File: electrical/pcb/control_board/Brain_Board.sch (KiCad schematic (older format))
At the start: 46 parts, among them J22 S9175-ND_rpi_breakout, J23 S9175-ND_rpi_breakout, J24 6posheader, J25 SSW-104-01-F-T, J26 WM6548-ND, J27 PPTC021LFBN-RC, J28 PPTC021LFBN-RC, J29 PPTC021LFBN-RC, J30 PEC08SAAN, M1 Mounting_Holes, Q1 2N3906, Q2 2N3906, Q3 2N3906, SW1 CT206124-ND, T13 test_point, T14 test_point, T15 test_point, U6 DC7G3HWA

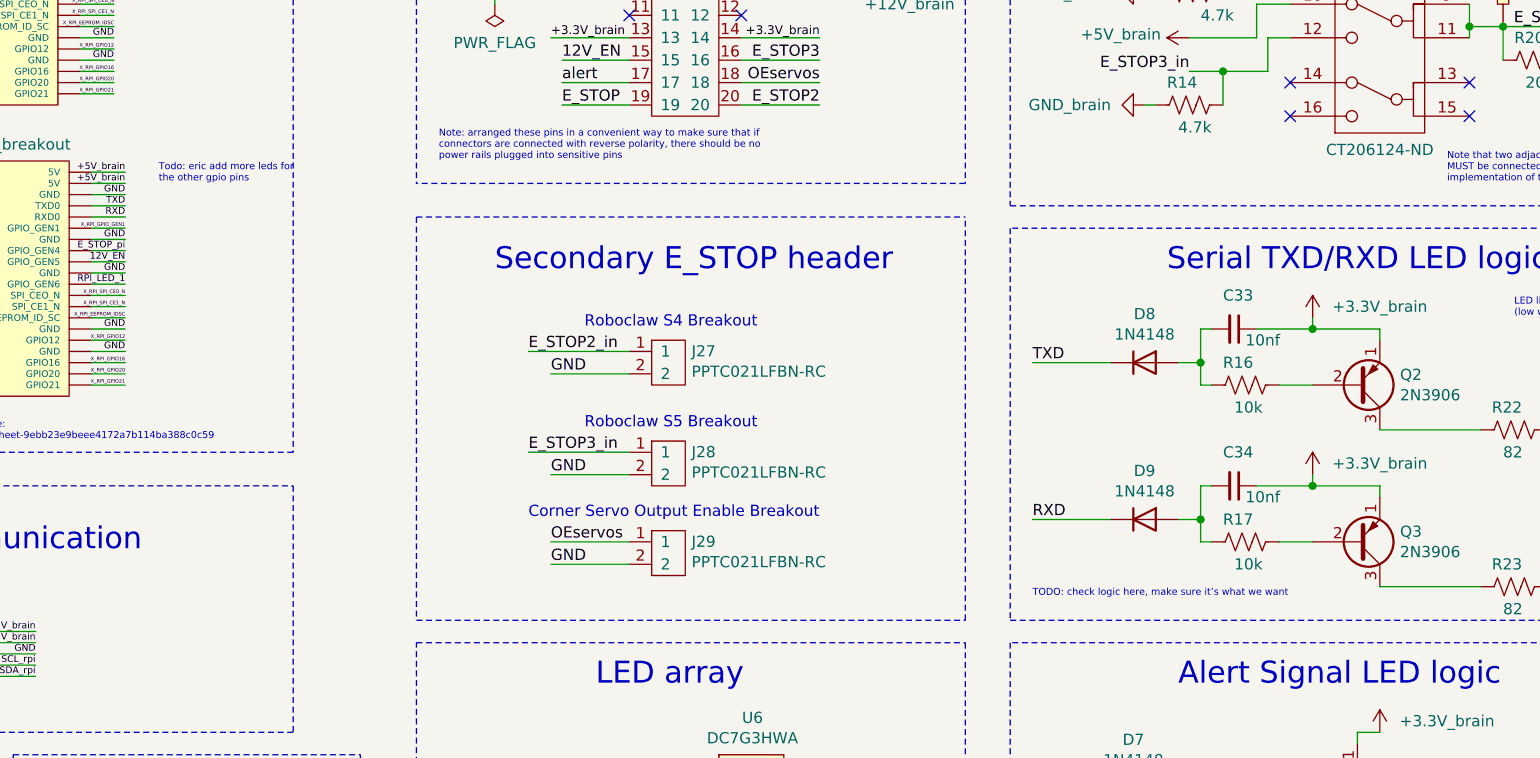
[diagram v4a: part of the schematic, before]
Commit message: deleting some todos
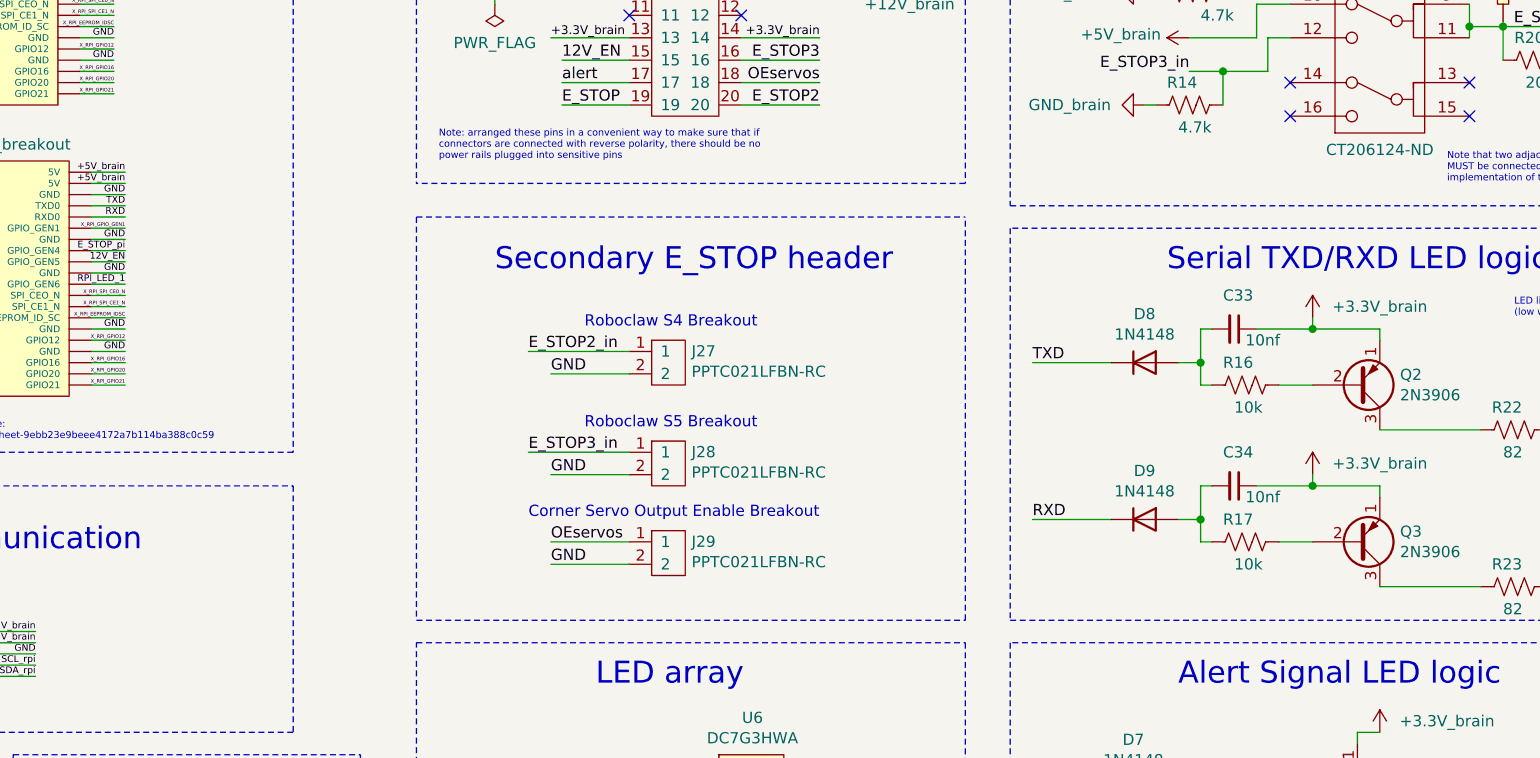
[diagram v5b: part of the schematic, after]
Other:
- note removed: "Todo: eric add more leds for \nthe other gpio pins"
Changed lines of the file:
@@
 Wire Wire Line
 	7900 2600 8200 2600
-Text Notes 3300 3250 0    31   ~ 0
-Todo: eric add more leds for \nthe other gpio pins
 Text Notes 9800 1500 0    31   ~ 0
 - Roboclaw ESTOPs active low \n(emergency stop when pulled low)\n- LEDs off when estop’ed (nominal on)
 Text Notes 7200 1450 0    31   ~ 0
 TODO: check logic here, make sure it’s what we want
-Text Notes 7200 5100 0    31   ~ 0
-TODO: check logic here, make sure it’s what we want
 $Comp

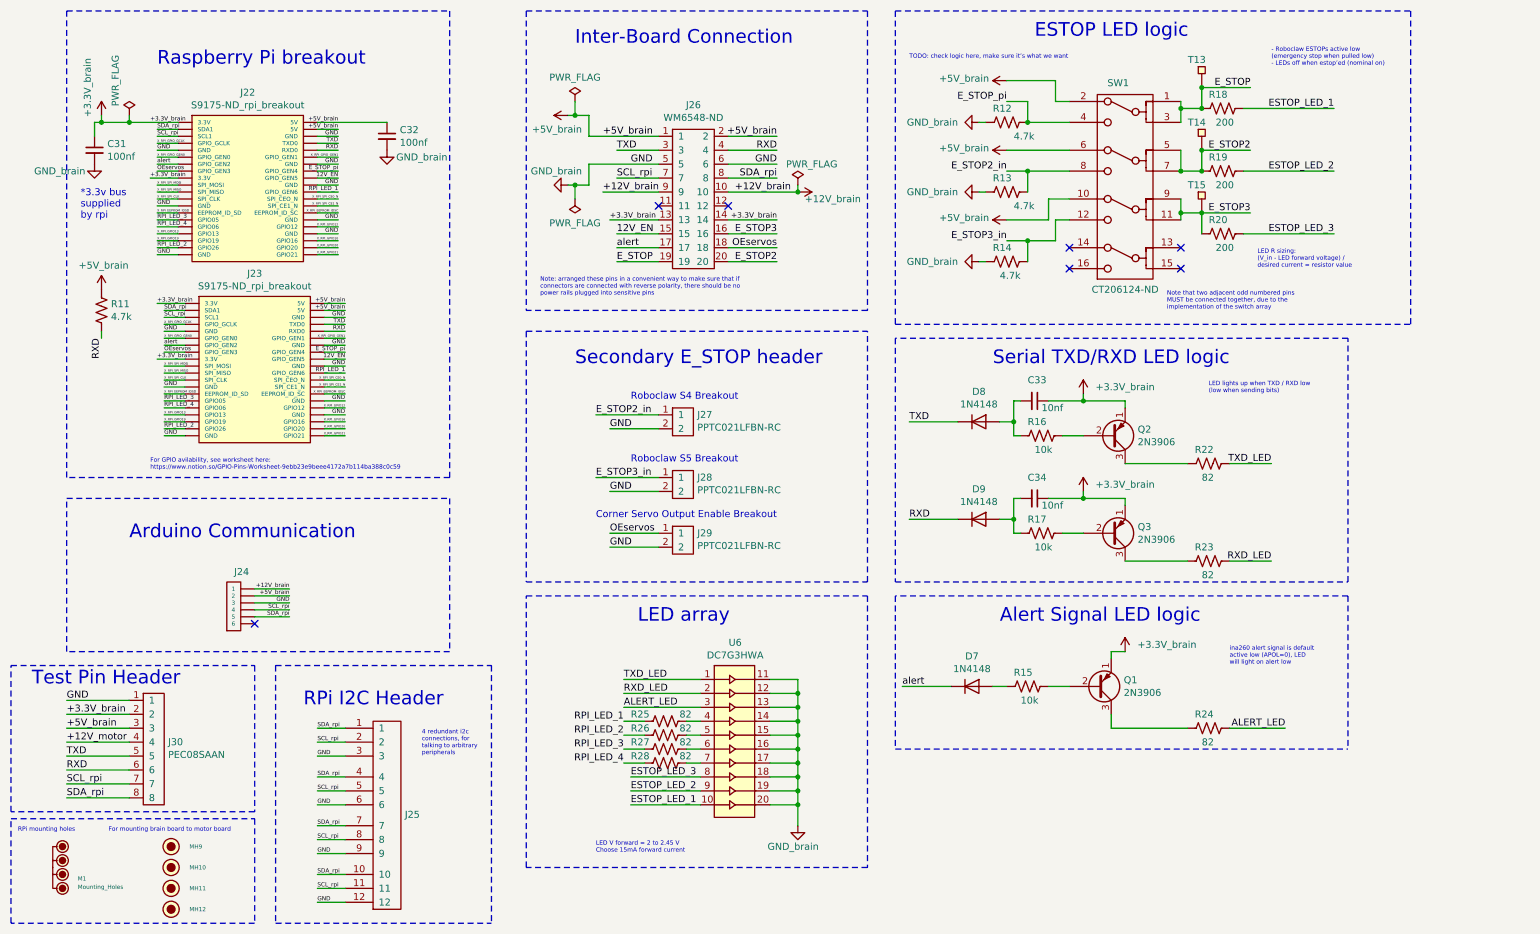
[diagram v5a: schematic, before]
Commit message: Moved alert LED to motor board, and moved estop pulldowns to have as an "option 2"
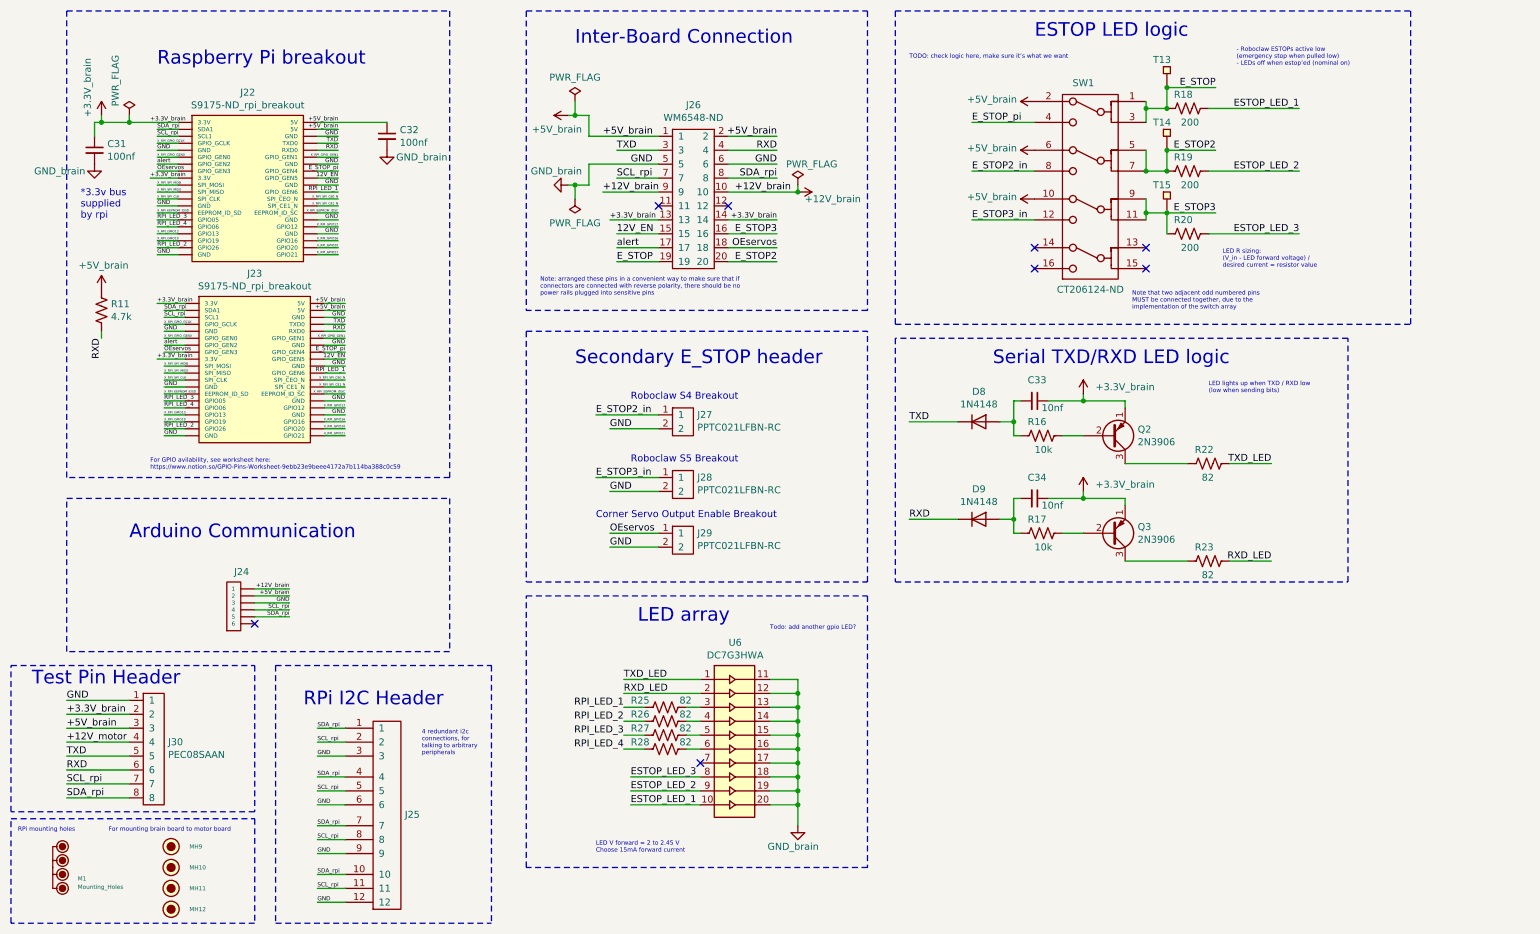
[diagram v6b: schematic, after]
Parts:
- removed D7: 1N4148, Diode_THT:D_DO-35_SOD27_P7.62mm_Horizontal, symbol Diode:1N4148
- removed Q1: 2N3906, Package_TO_SOT_THT:TO-92_Inline, symbol Transistor_BJT:2N3906
- removed R12, R13, R14: 4.7k, Resistor_THT:R_Axial_DIN0207_L6.3mm_D2.5mm_P7.62mm_Horizontal, symbol Device:R_US
- removed R15: 10k, Resistor_THT:R_Axial_DIN0207_L6.3mm_D2.5mm_P7.62mm_Horizontal, symbol Device:R_US
- removed R24: 82, Resistor_THT:R_Axial_DIN0207_L6.3mm_D2.5mm_P7.62mm_Horizontal, symbol Device:R_US
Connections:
- net ALERT_LED is gone; now on an unnamed net: U6.3
- net at R25.1: no longer U6.4
- net at R26.1: now also U6.4; no longer U6.5
- net at R27.1: now also U6.5; no longer U6.6
- net at R28.1: now also U6.6; no longer U6.7
- no-connect marks 7 -> 8
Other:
- note added: "Todo: add another gpio LED?"
- note removed: "Alert Signal LED logic"
- note removed: "ina260 alert signal is default \nactive low (APOL=0), LED \nwill light on alert low"
- moved on the sheet: R18, R19, R20, R25, R26, R27, R28, SW1, T13, T14, T15

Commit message: adding some notes from thursday convo
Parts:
- added Q?: 2N3906, Package_TO_SOT_THT:TO-92_Inline, symbol Transistor_BJT:2N3906
- added R?: 10k, Resistor_THT:R_Axial_DIN0207_L6.3mm_D2.5mm_P7.62mm_Horizontal, symbol Device:R_US
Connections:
- net +5V_brain: now also SW1.12 (out3_2), SW1.4 (out1_2), SW1.8 (out2_2); no longer SW1.10 (out3_1), SW1.2 (out1_1), SW1.6 (out2_1)
- net E_STOP: now also R?.2; no longer R18.2
- net E_STOP2_in: now also SW1.6 (out2_1); no longer SW1.8 (out2_2)
- net E_STOP3_in: now also SW1.10 (out3_1); no longer SW1.12 (out3_2)
- net E_STOP_pi: now also SW1.2 (out1_1); no longer SW1.4 (out1_2)
- new net: Q?.3 (C), R18.2
- new net: Q?.2 (B), R?.1
- new net 5v: Q?.1 (E)
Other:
- note added: "TODO: change left side to 3.3v?"
- note added: "TODO: use transistors for all 3 here"
- note added: "todo: use this setup for all LEDs driven by the PI. Basically pi is the ground/sink. LEDs will be default on when the pi turns on"
- note removed: "TODO: check logic here, make sure it’s what we want"
- moved on the sheet: R18
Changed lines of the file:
@@
 Wire Notes Line
 	4450 3400 6900 3400
-Text Label 7650 1900 0    50   ~ 0
+Text Label 7650 1750 0    50   ~ 0
 E_STOP_pi
 Wire Wire Line
@@
 Text Label 9400 2100 2    50   ~ 0
 E_STOP2
-Text Label 7650 2250 0    50   ~ 0
+Text Label 7650 2100 0    50   ~ 0
 E_STOP2_in
 Wire Wire Line
@@
 Text Label 9400 2550 2    50   ~ 0
 E_STOP3
-Text Label 7650 2600 0    50   ~ 0
+Text Label 7650 2450 0    50   ~ 0
 E_STOP3_in
 Wire Wire Line
@@
 L Device:R_US R?
 U 1 1 613A416D
-P 9200 1800
+P 10850 1850
 AR Path="/613A416D" Ref="R?"  Part="1"
 AR Path="/60A51BAC/613A416D" Ref="R?"  Part="1"
 AR Path="/60A5279E/613A416D" Ref="R18"  Part="1"
-F 0 "R18" V 9100 1700 50  0000 L CNN
-F 1 "200" V 9300 1750 50  0000 L CNN
-F 2 "Resistor_THT:R_Axial_DIN0207_L6.3mm_D2.5mm_P7.62mm_Horizontal" V 9240 1790 50  0001 C CNN
-F 3 "~" H 9200 1800 50  0001 C CNN
-	1    9200 1800
+F 0 "R18" V 10750 1750 50  0000 L CNN
+F 1 "200" V 10950 1800 50  0000 L CNN
+F 2 "Resistor_THT:R_Axial_DIN0207_L6.3mm_D2.5mm_P7.62mm_Horizontal" V 10890 1840 50  0001 C CNN
+F 3 "~" H 10850 1850 50  0001 C CNN
+	1    10850 1850
 	0    1    1    0
 $EndComp
 Text Label 9400 1650 2    50   ~ 0
 E_STOP
-Text Notes 9550 1500 0    31   ~ 0
+Text Notes 9450 1350 0    31   ~ 0
 - Roboclaw ESTOPs active low \n(emergency stop when pulled low)\n- LEDs off when estop’ed (nominal on)
 Text Notes 7200 1450 0    31   ~ 0
-TODO: check logic here, make sure it’s what we want
+TODO: change left side to 3.3v?
 $Comp
 L JPL_Robotics_Lib:SSW-104-01-F-T J25
@@
 Wire Wire Line
 	8900 1800 8900 1750
-Connection ~ 9050 1800
 Wire Wire Line
 	8900 2100 8900 2250
@@
 Text Notes 8800 3250 0    31   ~ 0
 Note that two adjacent odd numbered pins \nMUST be connected together, due to the \nimplementation of the switch array
-Text Label 10000 1800 2    50   ~ 0
+Text Label 11650 1850 2    50   ~ 0
 ESTOP_LED_1
 Wire Wire Line
-	9350 1800 10000 1800
-Wire Wire Line
-	9350 2250 10000 2250
-Wire Wire Line
-	9350 2700 10000 2700
+	11000 1850 11650 1850
 Text Label 10000 2250 2    50   ~ 0
 ESTOP_LED_2
@@
 L JPL_Robotics_Lib:+5V_brain #PWR069
 U 1 1 62FBEEB5
-P 8100 1750
-F 0 "#PWR069" H 8100 1600 50  0001 C CNN
-F 1 "+5V_brain" V 8115 1877 50  0000 L CNN
-F 2 "" H 8100 1750 50  0001 C CNN
-F 3 "" H 8100 1750 50  0001 C CNN
-	1    8100 1750
+P 8100 1900
+F 0 "#PWR069" H 8100 1750 50  0001 C CNN
+F 1 "+5V_brain" V 8115 2027 50  0000 L CNN
+F 2 "" H 8100 1900 50  0001 C CNN
+F 3 "" H 8100 1900 50  0001 C CNN
+	1    8100 1900
 	0    -1   -1   0
 $EndComp
@@
 L JPL_Robotics_Lib:+5V_brain #PWR070
 U 1 1 62FBF43E
-P 8100 2100
-F 0 "#PWR070" H 8100 1950 50  0001 C CNN
-F 1 "+5V_brain" V 8115 2227 50  0000 L CNN
-F 2 "" H 8100 2100 50  0001 C CNN
-F 3 "" H 8100 2100 50  0001 C CNN
-	1    8100 2100
+P 8100 2250
+F 0 "#PWR070" H 8100 2100 50  0001 C CNN
+F 1 "+5V_brain" V 8115 2377 50  0000 L CNN
+F 2 "" H 8100 2250 50  0001 C CNN
+F 3 "" H 8100 2250 50  0001 C CNN
+	1    8100 2250
 	0    -1   -1   0
 $EndComp
@@
 L JPL_Robotics_Lib:+5V_brain #PWR071
 U 1 1 62FBF7C3
-P 8100 2450
-F 0 "#PWR071" H 8100 2300 50  0001 C CNN
-F 1 "+5V_brain" V 8115 2577 50  0000 L CNN
-F 2 "" H 8100 2450 50  0001 C CNN
-F 3 "" H 8100 2450 50  0001 C CNN
-	1    8100 2450
+P 8100 2600
+F 0 "#PWR071" H 8100 2450 50  0001 C CNN
+F 1 "+5V_brain" V 8115 2727 50  0000 L CNN
+F 2 "" H 8100 2600 50  0001 C CNN
+F 3 "" H 8100 2600 50  0001 C CNN
+	1    8100 2600
 	0    -1   -1   0
 $EndComp
@@
 Todo: add another gpio LED?
 Wire Wire Line
-	8100 2600 7650 2600
-Wire Wire Line
-	8100 1900 7650 1900
-Wire Wire Line
-	8100 2250 7650 2250
+	8100 2450 7650 2450
+Wire Wire Line
+	8100 1750 7650 1750
+Wire Wire Line
+	8100 2100 7650 2100
+$Comp
+L Transistor_BJT:2N3906 Q?
+U 1 1 64ADE81C
+P 10300 1800
+F 0 "Q?" H 10490 1754 50  0000 L CNN
+F 1 "2N3906" H 10490 1845 50  0000 L CNN
+F 2 "Package_TO_SOT_THT:TO-92_Inline" H 10500 1725 50  0001 L CIN
+F 3 "https://www.onsemi.com/pub/Collateral/2N3906-D.PDF" H 10300 1800 50  0001 L CNN
+	1    10300 1800
+	1    0    0    1
+$EndComp
+Connection ~ 9050 1800
+Wire Wire Line
+	10400 2000 10700 2000
+Wire Wire Line
+	10700 2000 10700 1850
+Wire Wire Line
+	10400 1600 10400 1200
+Wire Wire Line
+	10400 1200 10450 1200
+Text Label 10450 1200 2    50   ~ 0
+5v
+$Comp
+L Device:R_US R?
+U 1 1 64C0012B
+P 9950 1800
+AR Path="/64C0012B" Ref="R?"  Part="1"
+AR Path="/60A51BAC/64C0012B" Ref="R?"  Part="1"
+AR Path="/60A5279E/64C0012B" Ref="R?"  Part="1"
+F 0 "R?" V 9850 1700 50  0000 L CNN
+F 1 "10k" V 10050 1750 50  0000 L CNN
+F 2 "Resistor_THT:R_Axial_DIN0207_L6.3mm_D2.5mm_P7.62mm_Horizontal" V 9990 1790 50  0001 C CNN
+F 3 "~" H 9950 1800 50  0001 C CNN
+	1    9950 1800
+	0    1    1    0
+$EndComp
+Wire Wire Line
+	9350 2700 10000 2700
+Wire Wire Line
+	9350 2250 10000 2250
+Wire Wire Line
+	9050 1800 9800 1800
+Text Label 3350 4150 0    50   ~ 0
+LEDfoo
+Text Label 3750 4150 0    50   ~ 0
+3.3v_reg
+Wire Wire Line
+	3200 4150 3750 4150
+Text Notes 10250 2400 0    31   ~ 0
+TODO: use transistors for all 3 here
+Text Notes 3500 3900 0    31   ~ 0
+todo: use this setup for all LEDs driven by the PI. Basically pi is the ground/sink. LEDs will be default on when the pi turns on
 $EndSCHEMATC
